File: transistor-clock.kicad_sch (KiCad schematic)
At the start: 58 parts, among them J1 Screw_Terminal_01x02, J2 Conn_01x01_Socket, J3 Conn_01x01_Socket, J4 Conn_01x01_Socket, J5 Conn_01x01_Socket, J6 Conn_01x01_Socket, J7 Conn_01x01_Socket, Q1 MMBT3904, Q10 MMBT3904, Q11 MMBT3904, Q12 MMBT3904, Q2 MMBT3904, Q3 MMBT3904, Q4 MMBT3904, Q5 AO3401A, Q6 2N7002, Q7 AO3401A, Q8 2N7002, Q9 MMBT3904, T1 Transformer_1P_SS, T2 CL2-20-12

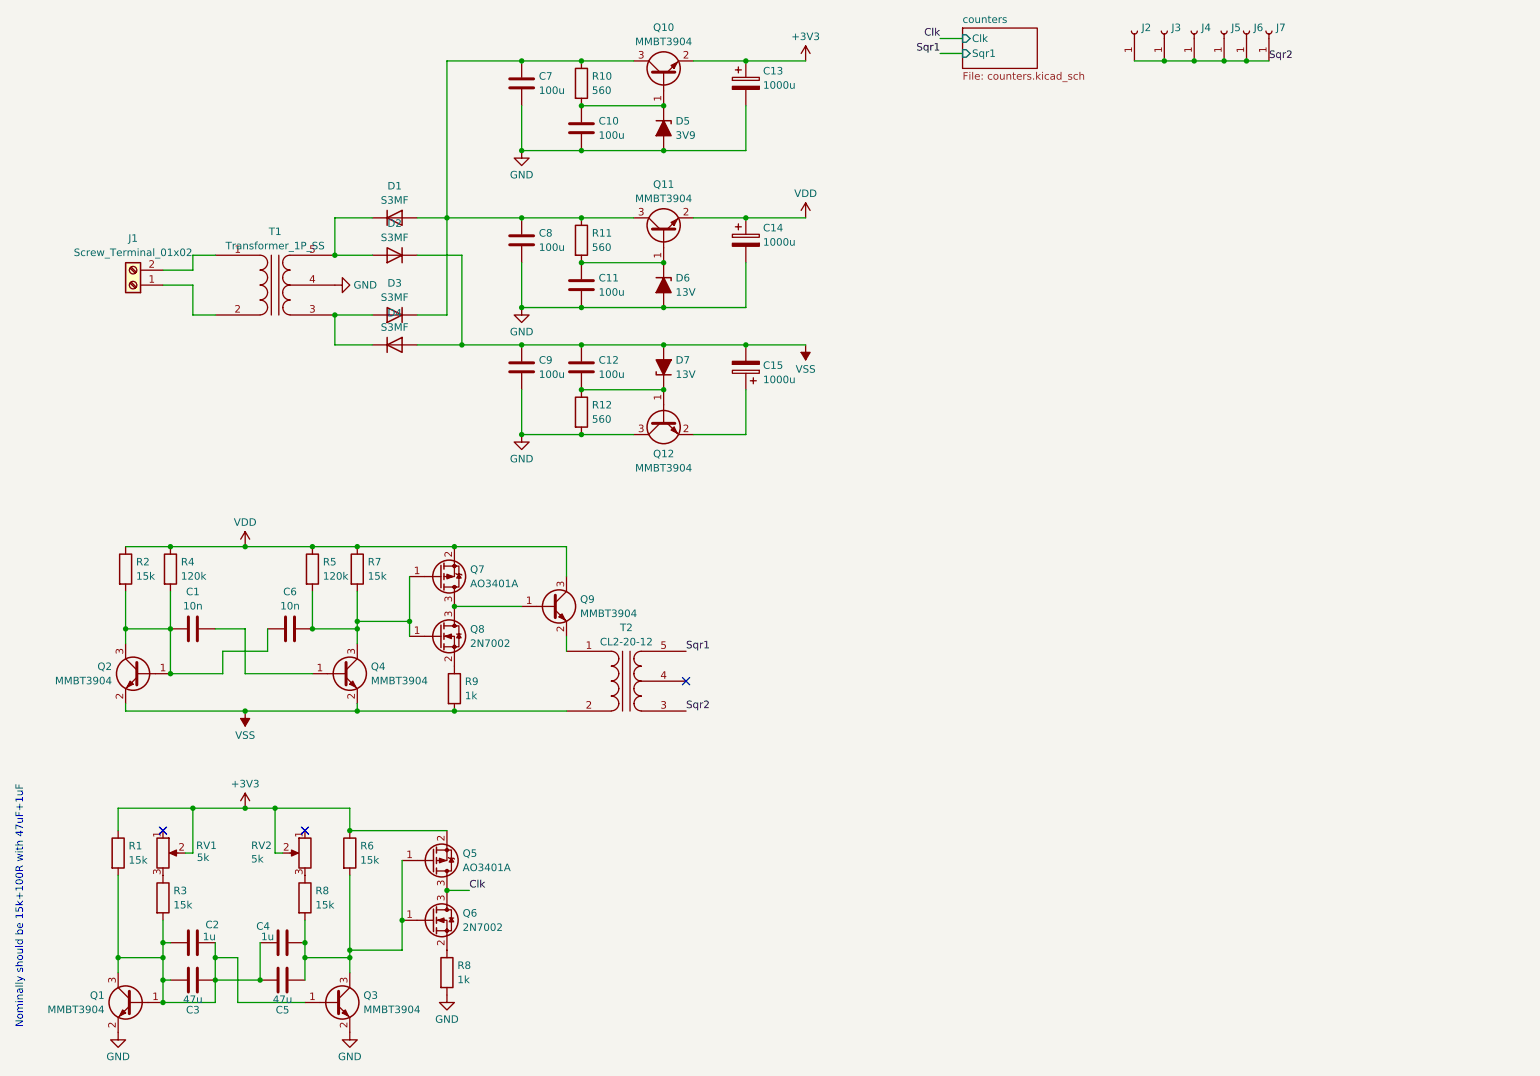
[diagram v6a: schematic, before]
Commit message: added module for PSU
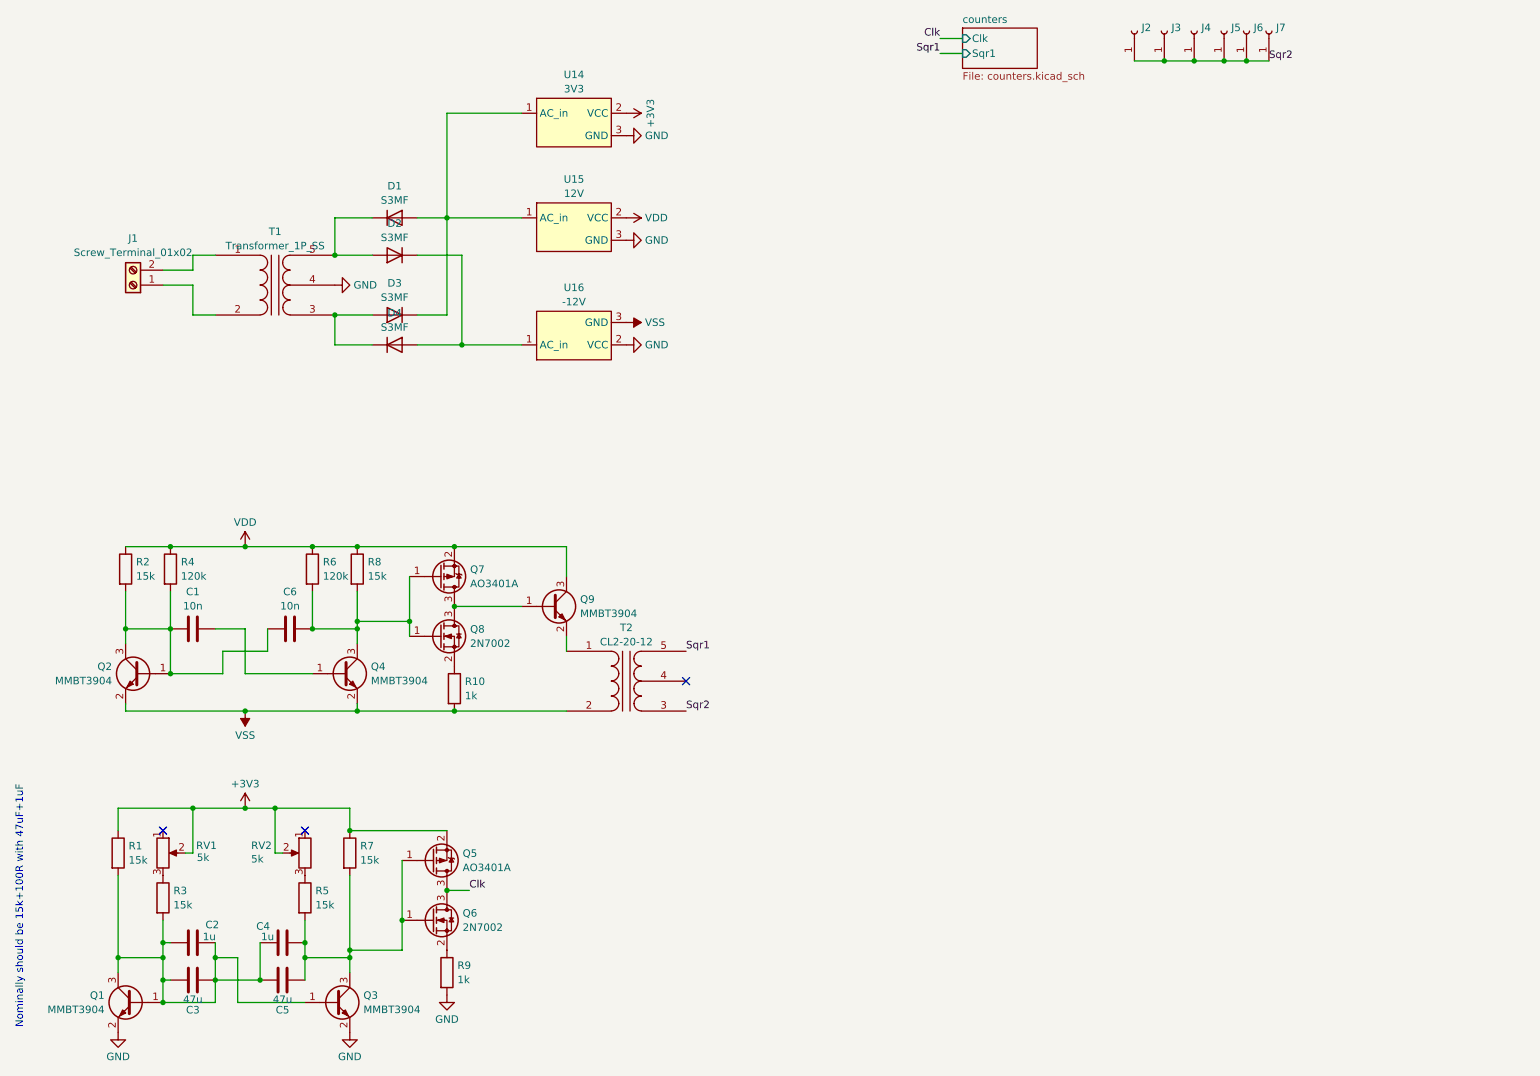
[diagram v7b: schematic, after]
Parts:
- removed C10, C11, C12, C7, C8, C9: 100u, Capacitor_Tantalum_SMD:CP_EIA-3528-12_Kemet-T, symbol Device:C
- removed C13, C14, C15: 1000u, Capacitor_SMD:CP_Elec_10x10.5, symbol Device:C_Polarized
- removed D5: 3V9, Diode_SMD:D_SOD-123, symbol Device:D_Zener_Filled
- removed D6, D7: 13V, Diode_SMD:D_SOD-123, symbol Device:D_Zener_Filled
- removed Q10, Q11, Q12: MMBT3904, Package_TO_SOT_SMD:SOT-23, symbol Transistor_BJT:MMBT3904
- removed R10, R11, R12: 560, Resistor_SMD:R_0402_1005Metric, symbol Device:R
- added U14: 3V3, custom:module_PSU, symbol custom:PSU
- added U15: 12V, custom:module_PSU, symbol custom:PSU
- added U16: -12V, custom:module_PSU, symbol custom:PSU
- renumbered R9 to R10, R8 to R5, R5 to R6, R6 to R7, R7 to R8, R8 to R9
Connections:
- net +3V3: now also U14.2 (VCC)
- net GND: now also U14.3 (GND), U15.3 (GND), U16.2 (VCC)
- net VDD: now also U15.2 (VCC)
- net VSS: now also U16.3 (GND); no longer D2.1 (K), D4.2 (A)
- net at D1.2 (A), D3.1 (K): now also U14.1 (AC_in), U15.1 (AC_in)
- new net: D2.1 (K), D4.2 (A), U16.1 (AC_in)

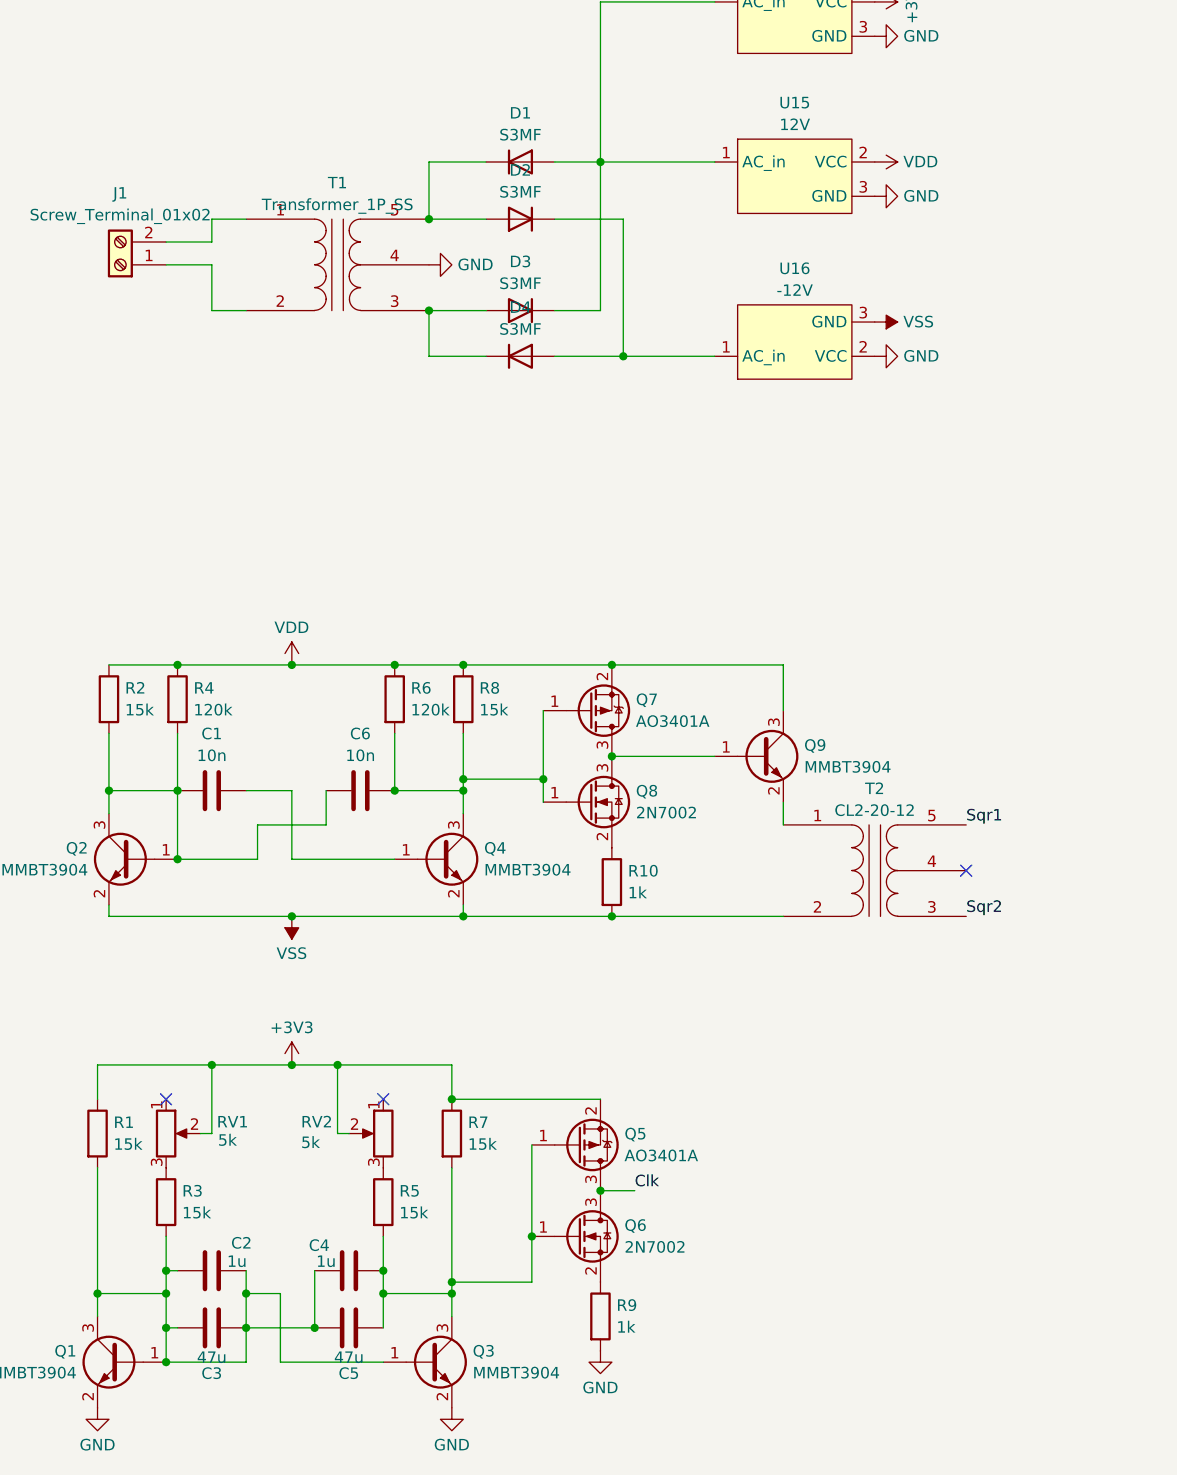
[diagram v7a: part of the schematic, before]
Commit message: some routing on main board
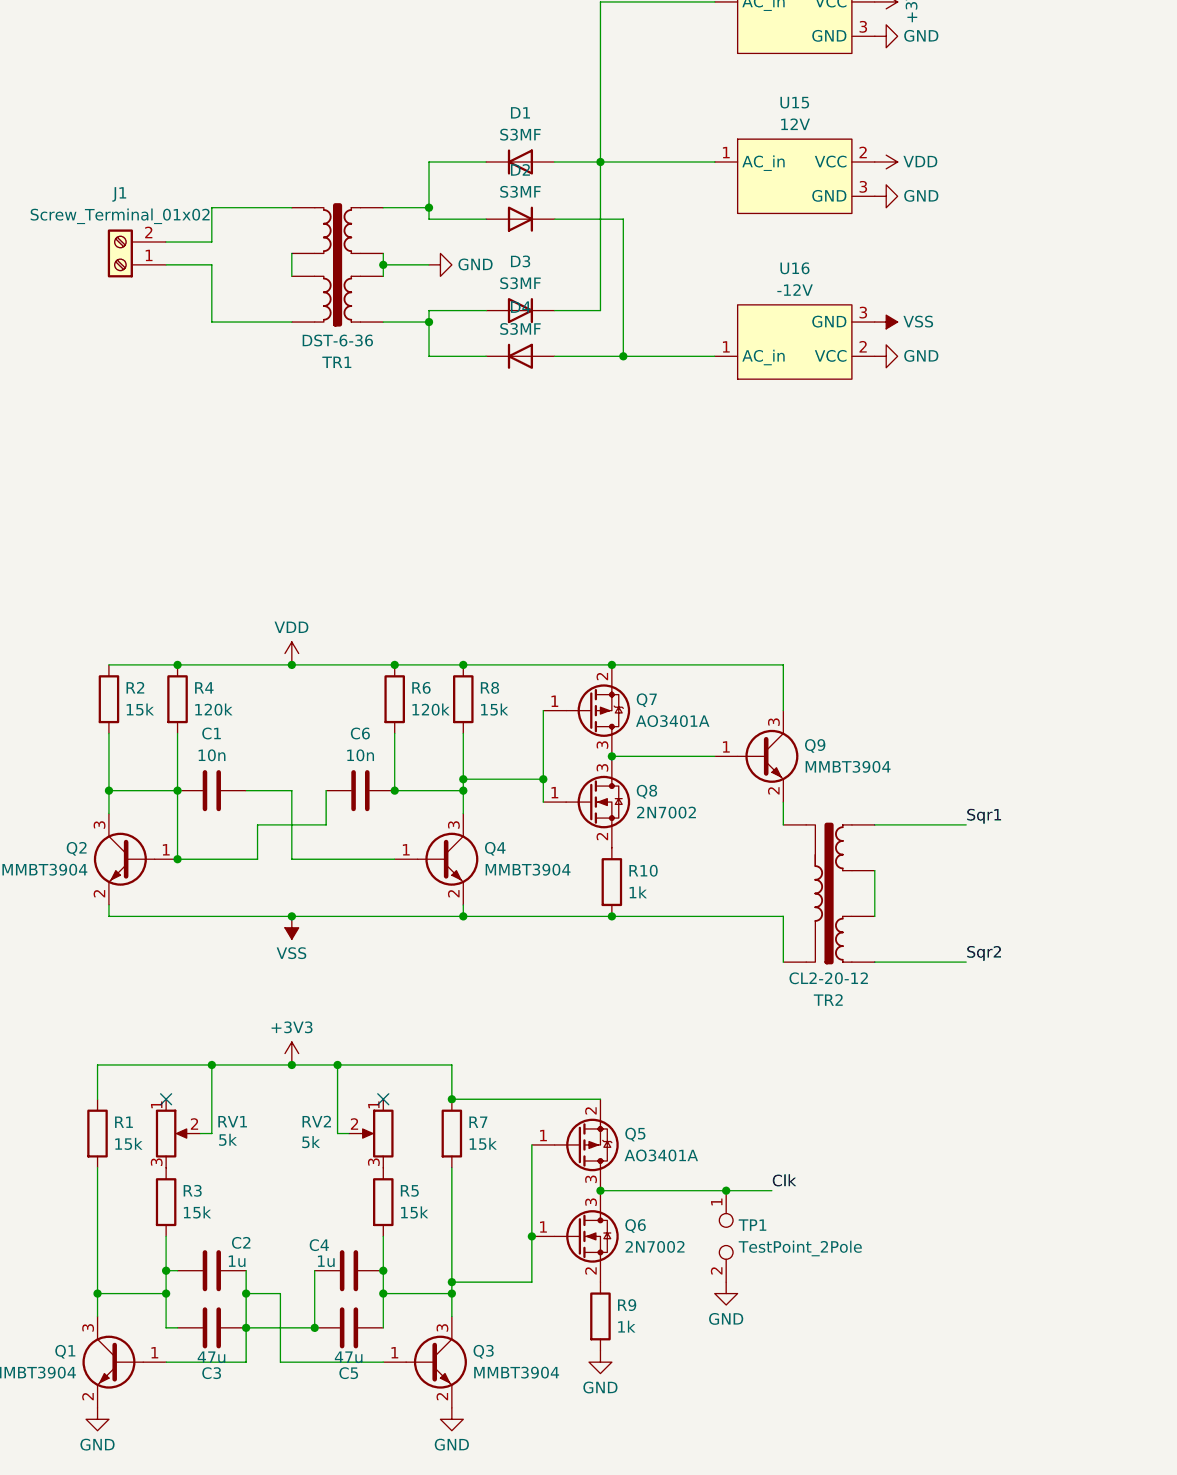
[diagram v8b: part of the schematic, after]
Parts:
- removed T1: Transformer_1P_SS, symbol Device:Transformer_1P_SS
- removed T2: CL2-20-12, symbol Device:Transformer_1P_SS
- added TP1: TestPoint_2Pole, Connector_PinHeader_2.54mm:PinHeader_1x02_P2.54mm_Vertical, symbol Connector:TestPoint_2Pole
- added TR1: DST-6-36, custom:DST-6-36, symbol Transformer:TRANSF6
- added TR2: CL2-20-12, custom:CL2-20-12, symbol Transformer:TRANSF3
- R1, R10, R2, R3, R4, R5, R6, R7, R8, R9: footprint Resistor_SMD:R_0402_1005Metric -> Resistor_SMD:R_0603_1608Metric
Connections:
- net Clk: now also TP1.1
- net GND: now also TP1.2, TR1.6, TR1.7
- net Sqr1: now also TR2.1
- net Sqr2: now also TR2.6
- net VSS: now also TR2.12
- net at D3.2 (A), D4.1 (K): now also TR1.8
- net at C2.2, C3.2, C4.1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: no longer C2.1, C3.1, Q1.3 (C), R1.2, R3.2
- net at Q9.2 (E): now also TR2.7
- net at J1.2 (Pin_2): now also TR1.4
- net at J1.1 (Pin_1): now also TR1.1
- net at D1.1 (K), D2.2 (A): now also TR1.5
- new net: C2.1, C3.1, Q1.3 (C), R1.2, R3.2
- new net: TR2.3, TR2.4
- new net: TR1.2, TR1.3
- no-connect marks 3 -> 2
